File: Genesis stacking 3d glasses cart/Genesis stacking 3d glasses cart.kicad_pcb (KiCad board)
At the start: 2 copper layers, 83.8 x 52.6 mm, 24 parts, among them CON1 GENESIS-EDGE, J1 Conn_01x32_Male, J2 Conn_01x32_Male, J3 top slot connector, J4 AudioJack3, U1 LM324, U2 74HC86, U3 74HC133, U4 74HC259

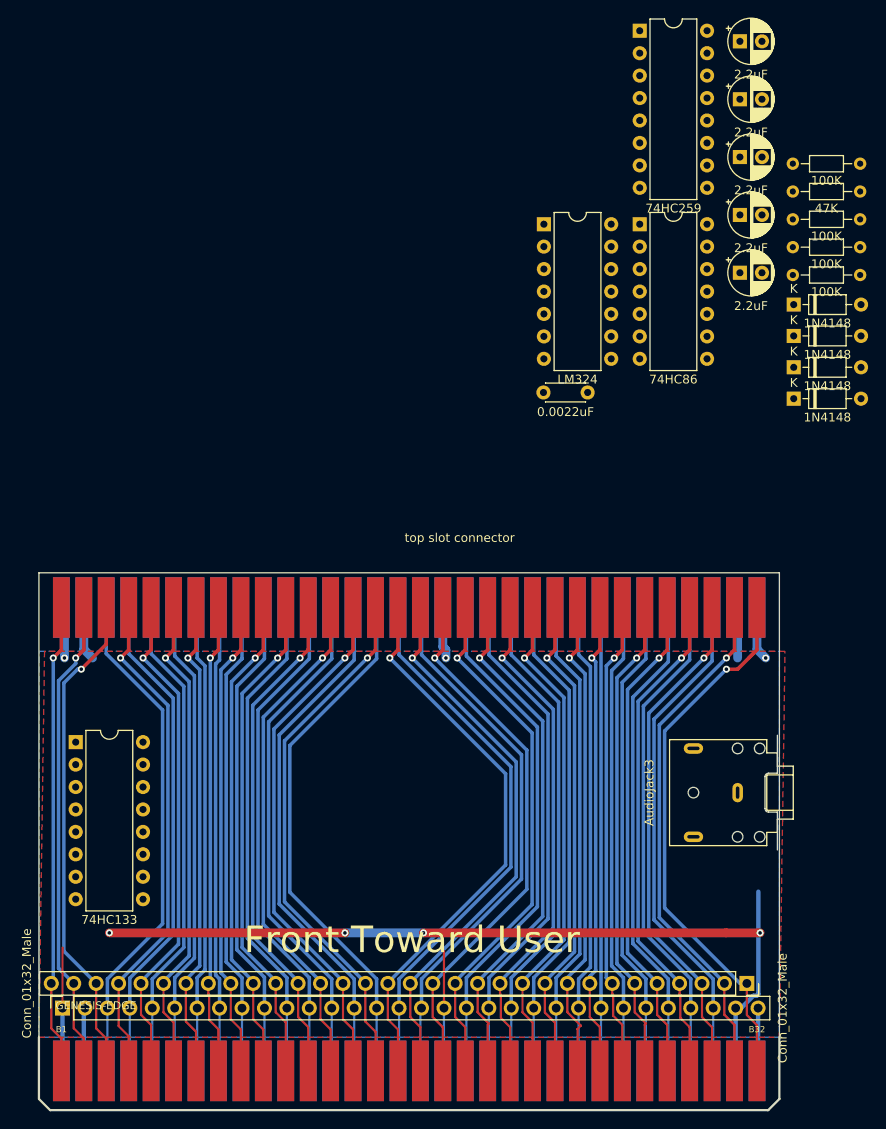
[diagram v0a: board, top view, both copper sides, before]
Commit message: added PTH version based on the incorrect schematic and the mostly SMD version based on the reverse engineered board someone made and tested.
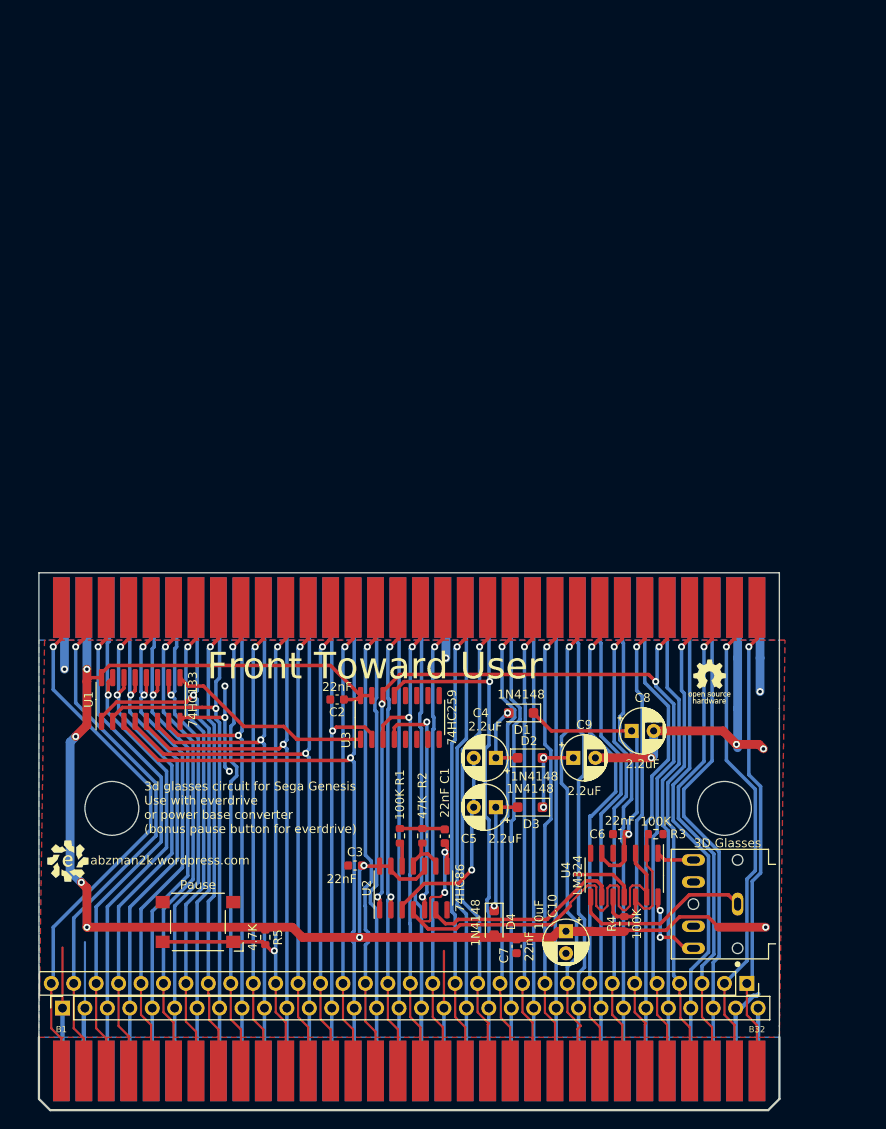
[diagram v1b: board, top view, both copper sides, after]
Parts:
- added C1: 22nF, Capacitor_SMD:C_0603_1608Metric, F.Cu at (130.0, 80.5)
- added C2: 22nF, Capacitor_SMD:C_0603_1608Metric, F.Cu at (117.9, 65.0)
- added C3: 22nF, Capacitor_SMD:C_0603_1608Metric, F.Cu at (119.9, 83.8)
- added C9: 2.2uF, Capacitor_THT:CP_Radial_D5.0mm_P2.50mm, F.Cu at (144.6, 71.6)
- added G***: LOGO, Evan's parts:OSHW gear, F.Cu at (160.0, 63.0)
- added G***: LOGO, Evan's parts:Evan Logo, F.Cu at (87.4, 83.3)
- added SW1: Pause, Button_Switch_SMD:SW_SPST_Omron_B3FS-105xP, F.Cu at (102.1, 90.2)
- C10: value 2.2uF -> 10uF
- C6, C7: value 2.2uF -> 22nF; footprint Capacitor_THT:CP_Radial_D5.0mm_P2.50mm -> Capacitor_SMD:C_0603_1608Metric
- C8: value 0.0022uF -> 2.2uF; footprint Capacitor_THT:C_Disc_D4.3mm_W1.9mm_P5.00mm -> Capacitor_THT:CP_Radial_D5.0mm_P2.50mm
- D1, D2, D3, D4: footprint Diode_THT:D_DO-35_SOD27_P7.62mm_Horizontal -> Diode_SMD:D_SOD-123F
- J4: value AudioJack3 -> 3D Glasses; footprint Connector_Audio:Jack_3.5mm_CUI_SJ1-3523N_Horizontal -> Evan's misc parts:CUI_SJ1-3525N
- R1, R2, R3, R4: footprint Resistor_THT:R_Axial_DIN0204_L3.6mm_D1.6mm_P7.62mm_Horizontal -> Resistor_SMD:R_0603_1608Metric
- R5: value 100K -> 4.7K; footprint Resistor_THT:R_Axial_DIN0204_L3.6mm_D1.6mm_P7.62mm_Horizontal -> Resistor_SMD:R_0603_1608Metric
- U1: value LM324 -> 74HC133; footprint Package_DIP:DIP-14_W7.62mm -> Package_SO:SOIC-16_3.9x9.9mm_P1.27mm
- U2: footprint Package_DIP:DIP-14_W7.62mm -> Package_SO:SOIC-14_3.9x8.7mm_P1.27mm
- U3: value 74HC133 -> 74HC259; footprint Package_DIP:DIP-16_W7.62mm -> Package_SO:SOIC-16_3.9x9.9mm_P1.27mm
- U4: value 74HC259 -> LM324; footprint Package_DIP:DIP-16_W7.62mm -> Package_SO:SOIC-14_3.9x8.7mm_P1.27mm
- moved R5 95.9 mm to (109.7, 91.9), turned to -90 degrees
- moved U4 95.6 mm to (150.4, 84.9), turned to -90 degrees
- moved R1 88.1 mm to (125.0, 80.5), turned to -90 degrees
- moved C7 86.6 mm to (138.2, 93.0), turned to 90 degrees
- moved C4 85.7 mm to (135.8, 71.6), turned to 180 degrees
- moved C5 84.8 mm to (135.8, 77.2), turned to 180 degrees
- moved R2 84.1 mm to (127.5, 80.5), turned to -90 degrees
- moved U2 79.4 mm to (126.5, 86.4), turned to 90 degrees
- moved R4 78.9 mm to (150.4, 90.4), turned to 90 degrees
- moved C6 77.8 mm to (149.9, 80.3)
- moved C10 77.1 mm to (143.8, 91.3), turned to -90 degrees
- moved R3 71.3 mm to (153.9, 80.3), turned to 180 degrees
- moved U1 70.6 mm to (95.6, 65.0), turned to 90 degrees
- moved D4 68.3 mm to (135.6, 90.3), turned to -90 degrees
- moved D3 58.1 mm to (139.7, 77.2), turned to 180 degrees
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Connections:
- C10 pad 1: Net-(D1-A) -> +5V
- C4 pad 1: Net-(D1-K) -> Net-(D1-A)
- C5 pad 1: Net-(D2-K) -> Net-(D3-A)
- C5 pad 2: +5V -> Net-(C4-Pad2)
- C6 pad 1: Net-(D3-K) -> GND
- C6 pad 2: Net-(C4-Pad2) -> Net-(D1-K)
- C7 pad 1: Net-(D4-K) -> GND
- C8 pad 1: GND -> Net-(D1-K)
- C8 pad 2: Net-(D4-K) -> +5V
- D2 pad 1: Net-(D2-K) -> Net-(D1-A)
- D2 pad 2: Net-(D1-K) -> Net-(D2-A)
- D3 pad 1: Net-(D3-K) -> Net-(D2-A)
- D3 pad 2: Net-(D2-K) -> Net-(D3-A)
- D4 pad 1: Net-(D4-K) -> Net-(D3-A)
- D4 pad 2: Net-(D3-K) -> +5V
- R1 pad 1: Net-(R1-Pad1) -> Net-(C1-Pad1)
- R2 pad 1: Net-(R1-Pad1) -> Net-(C1-Pad1)
- R3 pad 1: +5V -> GND
- R3 pad 2: Net-(U1A--) -> Net-(U4A--)
- R4 pad 1: GND -> +5V
- R4 pad 2: Net-(U1A--) -> Net-(U4A--)
- R5 pad 1: Net-(R1-Pad1) -> +5V
- R5 pad 2: Net-(U1A-+) -> /A23
- U1 pad 1: Net-(J4-PadR) -> /A5
- U1 pad 10: Net-(U1A--) -> /A11
- U1 pad 11: GND -> /A6
- U1 pad 12: Net-(U1A--) -> /A9
- U1 pad 13: Net-(U1A-+) -> /A10
- U1 pad 14: Net-(J4-PadT) -> /A8
- U1 pad 2: Net-(U1A--) -> /A12
- U1 pad 3: Net-(U1A-+) -> /A15
- U1 pad 4: Net-(D4-K) -> /A14
- U1 pad 5: GND -> /A3
- U1 pad 6: Net-(D4-K) -> /A13
- U1 pad 7: unconnected-(U1-Pad7) -> /A4
- U1 pad 8: Net-(J4-PadS) -> GND
- U1 pad 9: Net-(U1C--) -> Net-(U3-A0)
- U2 pad 4: Net-(U1A-+) -> Net-(U4A-+)
- U2 pad 5: Net-(U4-Q0) -> Net-(U3-Q0)
- U2 pad 6: Net-(U1C--) -> Net-(U4C--)
- U2 pad 8: Net-(U1A-+) -> Net-(U4A-+)
- U3 pad 1: /A3 -> Net-(U3-A0)
- U3 pad 10: /A10 -> unconnected-(U3-Q5-Pad10)
- U3 pad 11: /A11 -> unconnected-(U3-Q6-Pad11)
- U3 pad 12: /A12 -> unconnected-(U3-Q7-Pad12)
- U3 pad 13: /A13 -> /D0
- U3 pad 14: /A14 -> //WE
- U3 pad 15: /A15 -> +5V
- U3 pad 2: /A4 -> /A2
- U3 pad 3: /A5 -> //CE
- U3 pad 4: /A6 -> Net-(U3-Q0)
- U3 pad 5: /A7 -> unconnected-(U3-Q1-Pad5)
- U3 pad 6: /A8 -> unconnected-(U3-Q2-Pad6)
- U3 pad 7: /A9 -> unconnected-(U3-Q3-Pad7)
- U3 pad 9: Net-(U4-A0) -> unconnected-(U3-Q4-Pad9)
- U4 pad 1: Net-(U4-A0) -> Net-(J4-Pad2)
- U4 pad 10: unconnected-(U4-Q5-Pad10) -> Net-(U4A--)
- U4 pad 11: unconnected-(U4-Q6-Pad11) -> GND
- U4 pad 12: unconnected-(U4-Q7-Pad12) -> Net-(U4A--)
- U4 pad 13: unconnected-(U4-D-Pad13) -> Net-(U4A-+)
- U4 pad 14: //WE -> Net-(J4-Pad3)
- U4 pad 2: /A2 -> Net-(U4A--)
- U4 pad 3: unconnected-(U4-A2-Pad3) -> Net-(U4A-+)
- U4 pad 4: Net-(U4-Q0) -> Net-(D1-K)
- U4 pad 5: unconnected-(U4-Q1-Pad5) -> GND
- U4 pad 6: unconnected-(U4-Q2-Pad6) -> Net-(D1-K)
- U4 pad 8: GND -> Net-(J4-Pad1)
- U4 pad 9: unconnected-(U4-Q4-Pad9) -> Net-(U4C--)
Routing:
- net +5V: track 115.6 -> 236.7 mm, vias 4 -> 10
- net Net-(U4A-+): track 0.00 -> 60.4 mm, vias 0 -> 2
- net //WE: track 56.2 -> 112.6 mm, vias 1 -> 4
- net GND: track 52.7 -> 87.2 mm, vias 3 -> 6
- net Net-(D1-K): track 0.00 -> 31.5 mm, vias 0 -> 1
- net /A15: track 59.6 -> 88.1 mm, vias 0 -> 1
- net Net-(U3-Q0): track 0.00 -> 26.9 mm, vias 0 -> 2
- net /A14: track 57.4 -> 81.2 mm, vias 0 -> 1
- net Net-(U3-A0): track 0.00 -> 23.3 mm
- net Net-(U4C--): track 0.00 -> 23.2 mm
- net Net-(C4-Pad2): track 0.00 -> 22.8 mm, vias 0 -> 1
- net /A3: track 56.3 -> 77.3 mm, vias 0 -> 1
- net Net-(J4-Pad1): track 0.00 -> 20.7 mm
- net /A12: track 52.9 -> 72.7 mm, vias 0 -> 1
- net /A5: track 53.3 -> 73.1 mm, vias 0 -> 1
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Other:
- outline, holes or cut-outs redrawn
- board text added: "3d glasses circuit for Sega Genesis Use with everdrive or power base converter (bonus pause button for everdrive)"
- board text added: "Write to anywhere from 0xFFF8 to 0xFFFB set bit 0 high for the left eye low for right eye"
- board text added: "abzman2k.wordpress.com"

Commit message: updated silk
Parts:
- moved G*** 9.72 mm to (158.0, 72.5)
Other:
- board text added: "FRONT TOWARD ENEMY USER"
- board text removed: "Front Toward User"

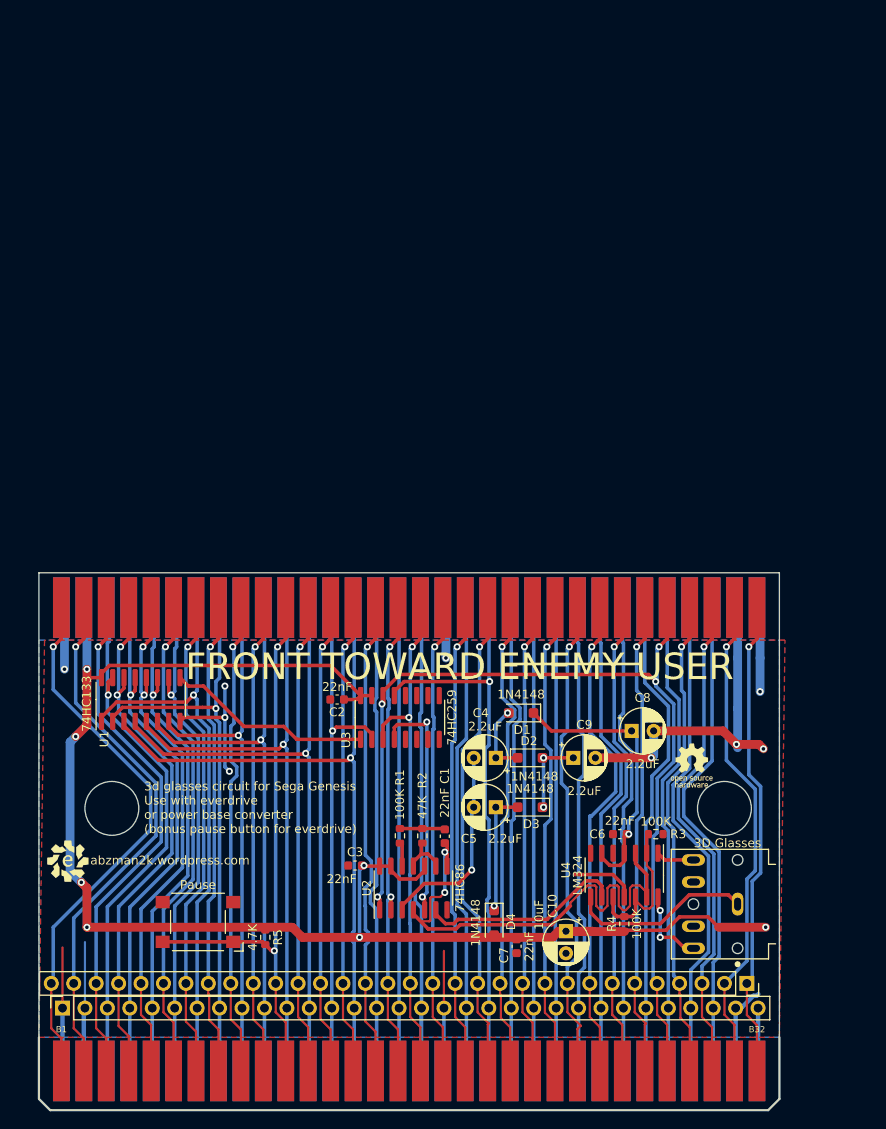
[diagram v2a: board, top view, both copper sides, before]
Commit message: updated design, added reference materials
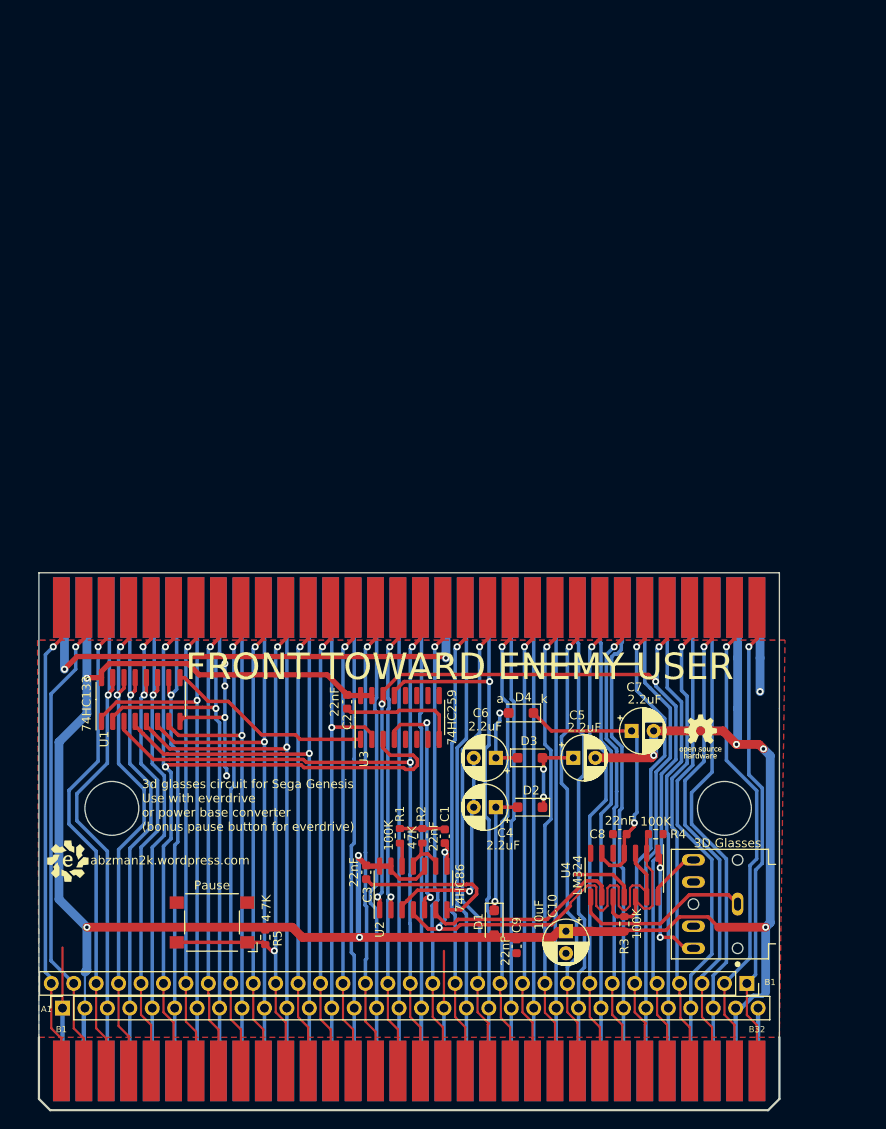
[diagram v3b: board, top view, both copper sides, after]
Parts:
- moved G*** 3.44 mm to (159.0, 69.2)
- moved SW1 1.59 mm to (103.7, 90.3)
- moved C3 1.48 mm to (121.2, 84.6), turned to 90 degrees
- moved C2 1.17 mm to (119.0, 65.3), turned to -90 degrees
- renumbered C5 to C4, C9 to C5, C4 to C6, C8 to C7, C6 to C8, C7 to C9, D4 to D1, D3 to D2, D2 to D3, D1 to D4, R4 to R3, R3 to R4
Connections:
- U1 pad 3: /A15 -> //CE
- U3 pad 3: //CE -> /A18
- U4 pad 1: Net-(J4-Pad2) -> Net-(J4-Pad3)
- U4 pad 14: Net-(J4-Pad3) -> Net-(J4-Pad2)
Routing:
- net GND: track 87.2 -> 165.3 mm, vias 6 -> 7
- net /A18: track 56.2 -> 89.2 mm, vias 1 -> 2
- net +5V: track 236.7 -> 268.3 mm, vias 10 -> 8
- net //CE: track 58.4 -> 88.8 mm
- net /A15: track 88.1 -> 60.0 mm, vias 1 -> 0
- net //SL1: track 62.5 -> 54.0 mm
- net //MRES: track 60.9 -> 55.5 mm
- net Net-(J4-Pad3): track 8.95 -> 13.9 mm
- net //SR1: track 59.3 -> 56.0 mm
- net /A7: track 67.7 -> 65.0 mm
- net /A8: track 60.8 -> 58.2 mm
- net Net-(U4A-+): track 60.4 -> 57.8 mm
- net /A9: track 59.7 -> 57.1 mm
- net /A10: track 66.4 -> 64.0 mm
- net /A6: track 65.5 -> 63.2 mm
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- removed copper zone on B.Cu, net +5V
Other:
- board text added: "a"
- board text added: "k"

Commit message: looks like last revision before fab
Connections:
- U4 pad 1: Net-(J4-Pad3) -> Net-(J4-Pad2)
- U4 pad 14: Net-(J4-Pad2) -> Net-(J4-Pad3)
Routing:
- net Net-(J4-Pad2): track 6.35 -> 4.33 mm
- net Net-(J4-Pad3): track 13.9 -> 12.5 mm
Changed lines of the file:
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@@
 			(layers "F.Cu" "F.Mask" "F.Paste")
 			(roundrect_rratio 0.25)
-			(net 85 "Net-(J4-Pad3)")
+			(net 82 "Net-(J4-Pad2)")
 			(pintype "output")
 		)
@@
 			(layers "F.Cu" "F.Mask" "F.Paste")
 			(roundrect_rratio 0.25)
-			(net 82 "Net-(J4-Pad2)")
+			(net 85 "Net-(J4-Pad3)")
 			(pintype "output")
 		)
@@
 	)
 	(segment
-		(start 127.136 89.861322)
-		(end 127.136 89.855751)
-		(width 0.25)
-		(layer "F.Cu")
-		(net 67)
-	)
-	(segment
 		(start 142.148 90.516)
 		(end 131.795528 90.516)
@@
 	)
 	(segment
-		(start 157.353 83.185)
-		(end 154.178 86.36)
+		(start 154.178 82.426)
+		(end 154.937 83.185)
 		(width 0.4)
 		(layer "F.Cu")
@@
 	)
 	(segment
-		(start 158.195 83.185)
-		(end 157.353 83.185)
-		(width 0.4)
-		(layer "F.Cu")
-		(net 82)
-	)
-	(segment
-		(start 154.178 86.36)
-		(end 154.178 87.376)
+		(start 154.937 83.185)
+		(end 158.195 83.185)
 		(width 0.4)
 		(layer "F.Cu")
@@
 	)
 	(segment
-		(start 154.432 84.074)
-		(end 154.432 82.68)
-		(width 0.4)
-		(layer "F.Cu")
-		(net 85)
-	)
-	(segment
 		(start 154.432 91.948)
 		(end 155.956 91.948)
@@
 	)
 	(segment
-		(start 154.432 82.68)
-		(end 154.178 82.426)
+		(start 154.178 85.852)
+		(end 154.432 85.598)
 		(width 0.4)
 		(layer "F.Cu")
@@
 		(net 85)
 	)
+	(segment
+		(start 154.178 87.376)
+		(end 154.178 85.852)
+		(width 0.4)
+		(layer "F.Cu")
+		(net 85)
+	)
 	(via
-		(at 154.432 84.074)
+		(at 154.432 85.598)
 		(size 0.8)
 		(drill 0.4)
@@
 	)
 	(segment
-		(start 154.432 91.948)
-		(end 154.432 84.074)
+		(start 154.432 85.598)
+		(end 154.432 91.948)
 		(width 0.4)
 		(layer "B.Cu")

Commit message: changes from ordering the pcb
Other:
- board text added: "A"
- board text added: "B"
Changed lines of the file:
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@@
 		(layer "Edge.Cuts")
 	)
-	(gr_text "A1"
-		(at 84.963 100.076 0)
+	(gr_text "A"
+		(at 85.09 100.076 0)
 		(layer "F.SilkS")
 		(effects
 			(font
-				(size 0.7 0.7)
-				(thickness 0.1)
+				(size 1 1)
+				(thickness 0.15)
 			)
 		)
@@
 		)
 	)
-	(gr_text "B1"
+	(gr_text "B"
 		(at 166.878 97.028 0)
 		(layer "F.SilkS")
 		(effects
 			(font
-				(size 0.7 0.7)
-				(thickness 0.1)
+				(size 1 1)
+				(thickness 0.15)
 			)
 		)
@@
 		(effects
 			(font
-				(size 0.7 0.7)
-				(thickness 0.1)
+				(size 1 1)
+				(thickness 0.15)
 			)
 		)
 	)
 	(gr_text "B1"
-		(at 86.645 102.368499 0)
+		(at 86.741 102.235 0)
 		(layer "F.SilkS")
 		(effects
 			(font
-				(size 0.7 0.7)
-				(thickness 0.1)
+				(size 1 1)
+				(thickness 0.15)
 			)
 		)
@@
 		(effects
 			(font
-				(size 0.7 0.7)
-				(thickness 0.1)
+				(size 1 1)
+				(thickness 0.15)
+			)
+			(justify mirror)
+		)
+	)
+	(gr_text "A"
+		(at 84.963 100.076 -0)
+		(layer "B.SilkS")
+		(effects
+			(font
+				(size 1 1)
+				(thickness 0.15)
 			)
 			(justify mirror)
@@
 		(effects
 			(font
-				(size 0.7 0.7)
-				(thickness 0.1)
+				(size 1 1)
+				(thickness 0.15)
 			)
 			(justify mirror)
@@
 		)
 	)
+	(gr_text "B"
+		(at 166.878 97.028 -0)
+		(layer "B.SilkS")
+		(effects
+			(font
+				(size 1 1)
+				(thickness 0.15)
+			)
+			(justify mirror)
+		)
+	)
